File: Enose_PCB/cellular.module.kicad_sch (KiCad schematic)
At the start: 40 parts, among them J7 U.FL-R-SMT_01_, J8 U.FL-R-SMT_01_, J9 2229333-2, Q1 Q_NPN, Q2 Q_NPN, Q3 Q_NPN, Q4 Q_NPN, Q5 Q_NPN, U4 SIM7070G

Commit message: Changed power symbols
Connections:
- net +BATT renamed +SYS_SW
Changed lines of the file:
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@@
 		(on_board yes)
 		(dnp no)
-		(fields_autoplaced yes)
-		(property "Reference" "#PWR0109"
+		(property "Reference" "#PWR090"
 			(at 229.87 33.02 0)
 			(effects
@@
 			)
 		)
-		(property "Value" "+BATT"
-			(at 237.49 33.0199 90)
+		(property "Value" "+SYS_SW"
+			(at 236.474 33.02 90)
 			(effects
 				(font
@@
 		)
 		(instances
-			(project ""
-				(path "/bf99c0e6-4ae6-4f18-a827-087a9b51b368"
-					(reference "#PWR08")
+			(project "Enose_PCB"
+				(path "/eef70be0-4107-491c-8ca0-465071a6397e/2117c019-44e0-44cf-b334-dcd1316d0701"
+					(reference "#PWR090")
 					(unit 1)
 				)
 			)
+		)
+	)
+	(symbol
+		(lib_id "power:+BATT")
+		(at 214.63 116.84 0)
+		(unit 1)
+		(exclude_from_sim no)
+		(in_bom yes)
+		(on_board yes)
+		(dnp no)
+		(property "Reference" "#PWR091"
+			(at 214.63 120.65 0)
+			(effects
+				(font
+					(size 1.27 1.27)
+				)
+				(hide yes)
+			)
+		)
+		(property "Value" "+SYS_SW"
+			(at 210.566 112.522 0)
+			(effects
+				(font
+					(size 1.27 1.27)
+				)
+				(justify left)
+			)
+		)
+		(property "Footprint" ""
+			(at 214.63 116.84 0)
+			(effects
+				(font
+					(size 1.27 1.27)
+				)
+				(hide yes)
+			)
+		)
+		(property "Datasheet" ""
+			(at 214.63 116.84 0)
+			(effects
+				(font
+					(size 1.27 1.27)
+				)
+				(hide yes)
+			)
+		)
+		(property "Description" "Power symbol creates a global label with name \"+BATT\""
+			(at 214.63 116.84 0)
+			(effects
+				(font
+					(size 1.27 1.27)
+				)
+				(hide yes)
+			)
+		)
+		(pin "1"
+		)
+		(instances
 			(project "Enose_PCB"
 				(path "/eef70be0-4107-491c-8ca0-465071a6397e/2117c019-44e0-44cf-b334-dcd1316d0701"
-					(reference "#PWR0109")
+					(reference "#PWR091")
 					(unit 1)
 				)
@@
 	)
 	(symbol
-		(lib_id "power:+BATT")
-		(at 266.7 116.84 0)
-		(unit 1)
-		(exclude_from_sim no)
-		(in_bom yes)
-		(on_board yes)
-		(dnp no)
-		(fields_autoplaced yes)
-		(property "Reference" "#PWR018"
-			(at 266.7 120.65 0)
-			(effects
-				(font
-					(size 1.27 1.27)
-				)
-				(hide yes)
-			)
-		)
-		(property "Value" "+BATT"
-			(at 266.7 111.76 0)
-			(effects
-				(font
-					(size 1.27 1.27)
-				)
-			)
-		)
-		(property "Footprint" ""
-			(at 266.7 116.84 0)
-			(effects
-				(font
-					(size 1.27 1.27)
-				)
-				(hide yes)
-			)
-		)
-		(property "Datasheet" ""
-			(at 266.7 116.84 0)
-			(effects
-				(font
-					(size 1.27 1.27)
-				)
-				(hide yes)
-			)
-		)
-		(property "Description" "Power symbol creates a global label with name \"+BATT\""
-			(at 266.7 116.84 0)
-			(effects
-				(font
-					(size 1.27 1.27)
-				)
-				(hide yes)
-			)
-		)
-		(pin "1"
-		)
-		(instances
-			(project "Enose_PCB"
-				(path "/eef70be0-4107-491c-8ca0-465071a6397e/2117c019-44e0-44cf-b334-dcd1316d0701"
-					(reference "#PWR018")
-					(unit 1)
-				)
-			)
-		)
-	)
-	(symbol
 		(lib_id "U.FL-R-SMT_01_:U.FL-R-SMT_01_")
 		(at 55.88 102.87 0)
@@
 	)
 	(symbol
+		(lib_id "power:+BATT")
+		(at 266.7 116.84 0)
+		(unit 1)
+		(exclude_from_sim no)
+		(in_bom yes)
+		(on_board yes)
+		(dnp no)
+		(property "Reference" "#PWR018"
+			(at 266.7 120.65 0)
+			(effects
+				(font
+					(size 1.27 1.27)
+				)
+				(hide yes)
+			)
+		)
+		(property "Value" "+SYS_SW"
+			(at 262.636 112.522 0)
+			(effects
+				(font
+					(size 1.27 1.27)
+				)
+				(justify left)
+			)
+		)
+		(property "Footprint" ""
+			(at 266.7 116.84 0)
+			(effects
+				(font
+					(size 1.27 1.27)
+				)
+				(hide yes)
+			)
+		)
+		(property "Datasheet" ""
+			(at 266.7 116.84 0)
+			(effects
+				(font
+					(size 1.27 1.27)
+				)
+				(hide yes)
+			)
+		)
+		(property "Description" "Power symbol creates a global label with name \"+BATT\""
+			(at 266.7 116.84 0)
+			(effects
+				(font
+					(size 1.27 1.27)
+				)
+				(hide yes)
+			)
+		)
+		(pin "1"
+		)
+		(instances
+			(project "Enose_PCB"
+				(path "/eef70be0-4107-491c-8ca0-465071a6397e/2117c019-44e0-44cf-b334-dcd1316d0701"
+					(reference "#PWR018")
+					(unit 1)
+				)
+			)
+		)
+	)
+	(symbol
 		(lib_id "power:GND")
 		(at 184.15 24.13 180)
@@
 					(unit 1)
 				)
-			)
-		)
-	)
-	(symbol
-		(lib_id "power:+BATT")
-		(at 214.63 116.84 0)
-		(unit 1)
-		(exclude_from_sim no)
-		(in_bom yes)
-		(on_board yes)
-		(dnp no)
-		(fields_autoplaced yes)
-		(property "Reference" "#PWR019"
-			(at 214.63 120.65 0)
-			(effects
-				(font
-					(size 1.27 1.27)
-				)
-				(hide yes)
-			)
-		)
-		(property "Value" "+BATT"
-			(at 214.63 111.76 0)
-			(effects
-				(font
-					(size 1.27 1.27)
-				)
-			)
-		)
-		(property "Footprint" ""
-			(at 214.63 116.84 0)
-			(effects
-				(font
-					(size 1.27 1.27)
-				)
-				(hide yes)
-			)
-		)
-		(property "Datasheet" ""
-			(at 214.63 116.84 0)
-			(effects
-				(font
-					(size 1.27 1.27)
-				)
-				(hide yes)
-			)
-		)
-		(property "Description" "Power symbol creates a global label with name \"+BATT\""
-			(at 214.63 116.84 0)
-			(effects
-				(font
-					(size 1.27 1.27)
-				)
-				(hide yes)
-			)
-		)
-		(pin "1"
-		)
-		(instances
-			(project "Enose_PCB"
-				(path "/eef70be0-4107-491c-8ca0-465071a6397e/2117c019-44e0-44cf-b334-dcd1316d0701"
-					(reference "#PWR019")
-					(unit 1)
-				)

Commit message: Working on Enose PCB Layout
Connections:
- net GND: now also Q1.2 (E), Q4.2 (E), Q5.2 (E); no longer Q1.E, Q4.E, Q5.E
- net UART1_RXD: now also Q2.2 (E); no longer Q2.E
- net UART1_TXD: now also Q3.3 (C); no longer Q3.C
- net at R16.2, R17.2: now also Q1.1 (B); no longer Q1.B
- net at C26.2, R20.1, U4.10 (UART1_RXD): now also Q2.3 (C); no longer Q2.C
- net at R27.2, R28.2: now also Q5.1 (B); no longer Q5.B
- net at R19.2: now also Q3.1 (B); no longer Q3.B
- net at U4.9 (UART1_TXD): now also Q3.2 (E); no longer Q3.E
- net at R18.2: now also Q2.1 (B); no longer Q2.B
- net at R25.2: now also Q4.3 (C); no longer Q4.C
- net at U4.1 (PWRKEY): now also Q1.3 (C); no longer Q1.C
- net at R21.2, R22.2: now also Q4.1 (B); no longer Q4.B
- net at R29.2: now also Q5.3 (C); no longer Q5.C
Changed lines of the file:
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@@
 		)
 	)
+	(netclass_flag ""
+		(length 2.54)
+		(shape round)
+		(at 157.48 33.02 0)
+		(fields_autoplaced yes)
+		(effects
+			(font
+				(size 1.27 1.27)
+			)
+			(justify left bottom)
+		)
+		(property "Netclass" "POWER_2A"
+			(at 158.1785 30.48 0)
+			(effects
+				(font
+					(size 1.27 1.27)
+				)
+				(justify left)
+				(hide yes)
+			)
+		)
+		(property "Component Class" ""
+			(at -109.22 0 0)
+			(effects
+				(font
+					(size 1.27 1.27)
+					(italic yes)
+				)
+			)
+		)
+	)
 	(symbol
 		(lib_id "power:GND")
@@
 			)
 		)
-		(pin "E"
+		(pin "1"
 		)
-		(pin "C"
+		(pin "3"
 		)
-		(pin "B"
+		(pin "2"
 		)
 		(instances
@@
 	)
 	(symbol
+		(lib_name "Q_NPN_4")
 		(lib_id "Device:Q_NPN")
 		(at 73.66 58.42 270)
@@
 			)
 		)
-		(pin "E"
+		(pin "2"
 		)
-		(pin "C"
+		(pin "1"
 		)
-		(pin "B"
+		(pin "3"
 		)
 		(instances
@@
 	)
 	(symbol
+		(lib_name "Q_NPN_3")
 		(lib_id "Device:Q_NPN")
 		(at 54.61 40.64 0)
@@
 			)
 		)
-		(pin "E"
+		(pin "1"
 		)
-		(pin "C"
+		(pin "3"
 		)
-		(pin "B"
+		(pin "2"
 		)
 		(instances
@@
 	)
 	(symbol
+		(lib_name "Q_NPN_2")
 		(lib_id "Device:Q_NPN")
 		(at 264.16 139.7 0)
@@
 			)
 		)
-		(pin "E"
+		(pin "2"
 		)
-		(pin "C"
+		(pin "3"
 		)
-		(pin "B"
+		(pin "1"
 		)
 		(instances
@@
 	)
 	(symbol
+		(lib_name "Q_NPN_1")
 		(lib_id "Device:Q_NPN")
 		(at 212.09 139.7 0)
@@
 			)
 		)
-		(pin "E"
+		(pin "1"
 		)
-		(pin "C"
+		(pin "3"
 		)
-		(pin "B"
+		(pin "2"
 		)
 		(instances

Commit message: Enose PCB almost done
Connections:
- net UART1_RXD: now also Q3.3 (C); no longer Q2.2 (E)
- net UART1_TXD: now also Q2.2 (E); no longer Q3.3 (C)
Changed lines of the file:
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@@
+	(wire
+		(pts
+			(xy 266.7 144.78) (xy 266.7 148.59)
+		)
+		(stroke
+			(width 0)
+			(type default)
+		)
+	)
+	(wire
+		(pts
+			(xy 101.6 91.44) (xy 102.87 91.44)
+		)
+		(stroke
+			(width 0)
+			(type default)
+		)
+	)
+	(wire
+		(pts
+			(xy 266.7 148.59) (xy 266.7 149.86)
+		)
+		(stroke
+			(width 0)
+			(type default)
+		)
+	)
+	(wire
+		(pts
+			(xy 163.83 31.75) (xy 163.83 33.02)
+		)
+		(stroke
+			(width 0)
+			(type default)
+		)
+	)
+	(wire
+		(pts
+			(xy 86.36 46.99) (xy 73.66 46.99)
+		)
+		(stroke
+			(width 0)
+			(type default)
+		)
+	)
+	(wire
+		(pts
+			(xy 223.52 63.5) (xy 223.52 66.04)
+		)
+		(stroke
+			(width 0)
+			(type default)
+		)
+	)
+	(wire
+		(pts
+			(xy 198.12 68.58) (xy 208.28 68.58)
+		)
+		(stroke
+			(width 0)
+			(type default)
+		)
+	)
+	(wire
+		(pts
+			(xy 254 148.59) (xy 254 139.7)
+		)
+		(stroke
+			(width 0)
+			(type default)
+		)
+	)
+	(wire
+		(pts
+			(xy 219.71 73.66) (xy 228.6 73.66)
+		)
+		(stroke
+			(width 0)
+			(type default)
+		)
+	)
+	(wire
+		(pts
+			(xy 86.36 60.96) (xy 96.52 60.96)
+		)
+		(stroke
+			(width 0)
+			(type default)
+		)
+	)
+	(wire
+		(pts
+			(xy 102.87 66.04) (xy 99.06 66.04)
+		)
+		(stroke
+			(width 0)
+			(type default)
+		)
+	)
+	(wire
+		(pts
+			(xy 186.69 68.58) (xy 190.5 68.58)
+		)
+		(stroke
+			(width 0)
+			(type default)
+		)
+	)
+	(wire
+		(pts
+			(xy 99.06 68.58) (xy 93.98 68.58)
+		)
+		(stroke
+			(width 0)
+			(type default)
+		)
+	)
+	(wire
+		(pts
+			(xy 163.83 33.02) (xy 173.99 33.02)
+		)
+		(stroke
+			(width 0)
+			(type default)
+		)
+	)
+	(wire
+		(pts
+			(xy 266.7 148.59) (xy 261.62 148.59)
+		)
+		(stroke
+			(width 0)
+			(type default)
+		)
+	)
+	(wire
+		(pts
+			(xy 274.32 71.12) (xy 274.32 73.66)
+		)
+		(stroke
+			(width 0)
+			(type default)
+		)
+	)
+	(wire
+		(pts
+			(xy 203.2 78.74) (xy 203.2 83.82)
+		)
+		(stroke
+			(width 0)
+			(type default)
+		)
+	)
+	(wire
+		(pts
+			(xy 152.4 35.56) (xy 152.4 33.02)
+		)
+		(stroke
+			(width 0)
+			(type default)
+		)
+	)
+	(wire
+		(pts
+			(xy 44.45 100.33) (xy 45.72 100.33)
+		)
+		(stroke
+			(width 0)
+			(type default)
+		)
+	)
+	(wire
+		(pts
+			(xy 184.15 33.02) (xy 195.58 33.02)
+		)
+		(stroke
+			(width 0)
+			(type default)
+		)
+	)
 	(wire
 		(pts
@@
 	(wire
 		(pts
-			(xy 266.7 144.78) (xy 266.7 148.59)
-		)
-		(stroke
-			(width 0)
-			(type default)
-		)
-	)
-	(wire
-		(pts
-			(xy 101.6 91.44) (xy 102.87 91.44)
-		)
-		(stroke
-			(width 0)
-			(type default)
-		)
-	)
-	(wire
-		(pts
-			(xy 266.7 148.59) (xy 266.7 149.86)
-		)
-		(stroke
-			(width 0)
-			(type default)
-		)
-	)
-	(wire
-		(pts
-			(xy 163.83 31.75) (xy 163.83 33.02)
-		)
-		(stroke
-			(width 0)
-			(type default)
-		)
-	)
-	(wire
-		(pts
-			(xy 86.36 46.99) (xy 73.66 46.99)
-		)
-		(stroke
-			(width 0)
-			(type default)
-		)
-	)
-	(wire
-		(pts
-			(xy 223.52 63.5) (xy 223.52 66.04)
-		)
-		(stroke
-			(width 0)
-			(type default)
-		)
-	)
-	(wire
-		(pts
-			(xy 198.12 68.58) (xy 208.28 68.58)
-		)
-		(stroke
-			(width 0)
-			(type default)
-		)
-	)
-	(wire
-		(pts
-			(xy 254 148.59) (xy 254 139.7)
-		)
-		(stroke
-			(width 0)
-			(type default)
-		)
-	)
-	(wire
-		(pts
-			(xy 219.71 73.66) (xy 228.6 73.66)
-		)
-		(stroke
-			(width 0)
-			(type default)
-		)
-	)
-	(wire
-		(pts
-			(xy 86.36 60.96) (xy 96.52 60.96)
-		)
-		(stroke
-			(width 0)
-			(type default)
-		)
-	)
-	(wire
-		(pts
-			(xy 102.87 66.04) (xy 99.06 66.04)
-		)
-		(stroke
-			(width 0)
-			(type default)
-		)
-	)
-	(wire
-		(pts
-			(xy 186.69 68.58) (xy 190.5 68.58)
-		)
-		(stroke
-			(width 0)
-			(type default)
-		)
-	)
-	(wire
-		(pts
-			(xy 99.06 68.58) (xy 93.98 68.58)
-		)
-		(stroke
-			(width 0)
-			(type default)
-		)
-	)
-	(wire
-		(pts
-			(xy 163.83 33.02) (xy 173.99 33.02)
-		)
-		(stroke
-			(width 0)
-			(type default)
-		)
-	)
-	(wire
-		(pts
-			(xy 266.7 148.59) (xy 261.62 148.59)
-		)
-		(stroke
-			(width 0)
-			(type default)
-		)
-	)
-	(wire
-		(pts
-			(xy 274.32 71.12) (xy 274.32 73.66)
-		)
-		(stroke
-			(width 0)
-			(type default)
-		)
-	)
-	(wire
-		(pts
-			(xy 203.2 78.74) (xy 203.2 83.82)
-		)
-		(stroke
-			(width 0)
-			(type default)
-		)
-	)
-	(wire
-		(pts
-			(xy 152.4 35.56) (xy 152.4 33.02)
-		)
-		(stroke
-			(width 0)
-			(type default)
-		)
-	)
-	(wire
-		(pts
-			(xy 44.45 100.33) (xy 45.72 100.33)
-		)
-		(stroke
-			(width 0)
-			(type default)
-		)
-	)
-	(wire
-		(pts
-			(xy 184.15 33.02) (xy 195.58 33.02)
-		)
-		(stroke
-			(width 0)
-			(type default)
-		)
-	)
-	(wire
-		(pts
 			(xy 224.79 33.02) (xy 229.87 33.02)
 		)
@@
 	(wire
 		(pts
+			(xy 64.77 68.58) (xy 83.82 68.58)
+		)
+		(stroke
+			(width 0)
+			(type default)
+		)
+	)
+	(wire
+		(pts
 			(xy 101.6 86.36) (xy 102.87 86.36)
 		)
@@
 		(pts
 			(xy 148.59 114.3) (xy 148.59 116.84)
-		)
-		(stroke
-			(width 0)
-			(type default)
-		)
-	)
-	(wire
-		(pts
-			(xy 64.77 68.58) (xy 83.82 68.58)
 		)
 		(stroke
@@
 	(global_label "UART1_TXD"
 		(shape input)
-		(at 64.77 68.58 180)
+		(at 64.77 60.96 180)
 		(fields_autoplaced yes)
 		(effects
@@
 		)
 		(property "Intersheetrefs" "${INTERSHEET_REFS}"
-			(at 51.5039 68.58 0)
+			(at 51.5039 60.96 0)
 			(effects
 				(font
@@
 	(global_label "UART1_RXD"
 		(shape input)
-		(at 64.77 60.96 180)
+		(at 64.77 68.58 180)
 		(fields_autoplaced yes)
 		(effects
@@
 		)
 		(property "Intersheetrefs" "${INTERSHEET_REFS}"
-			(at 51.2015 60.96 0)
+			(at 51.2015 68.58 0)
 			(effects
 				(font

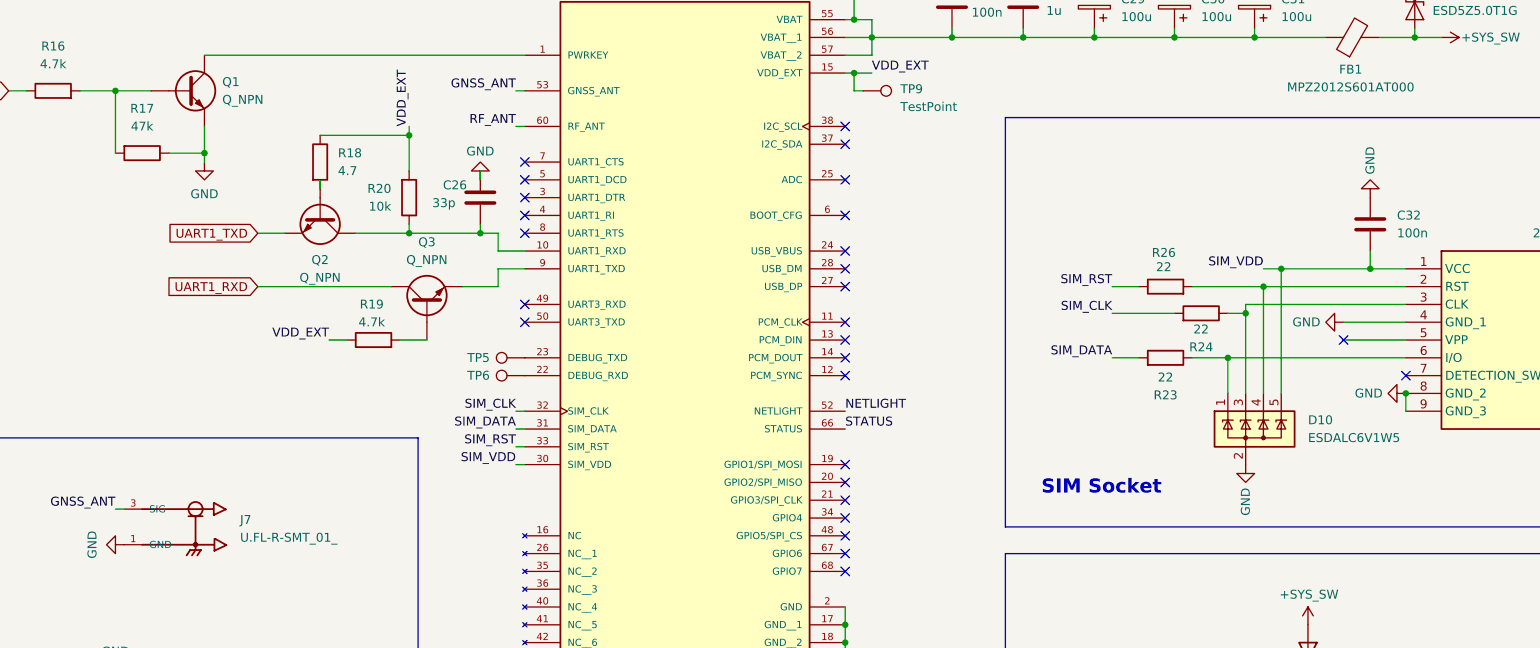
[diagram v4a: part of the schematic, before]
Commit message: Enose PCB almost done, just needs ground vias
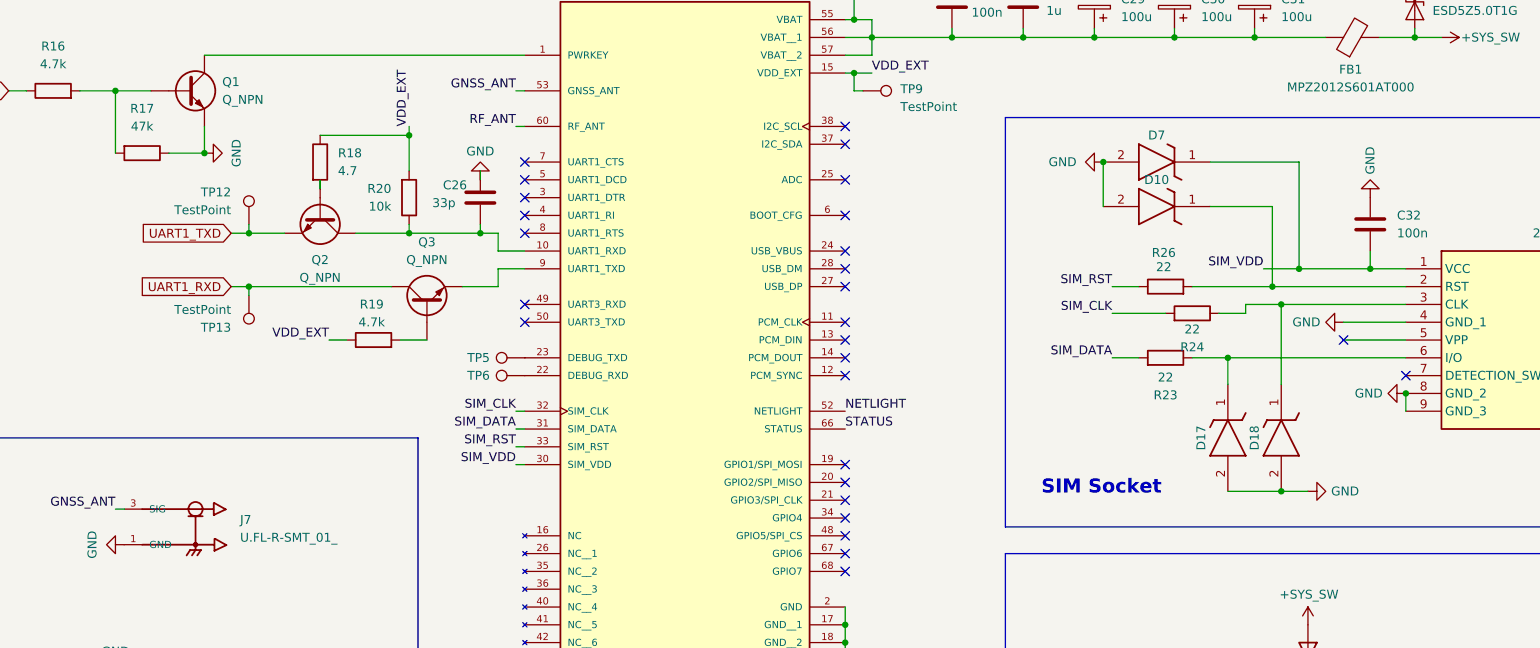
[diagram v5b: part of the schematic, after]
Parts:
- removed D10: ESDALC6V1W5, ESDALC6V1W5:SOT65P210X110-5N, symbol Power_Protection:SP0504BAHT
- added D10, D17, D18, D7: ESD8351XV2T1G, SamacSys_Parts:SODFL1608X70N, symbol SamacSys_Parts:ESD8351XV2T1G
- added TP12, TP13: TestPoint, TestPoint:TestPoint_Pad_D1.5mm, symbol Connector:TestPoint
- TP5, TP6, TP8, TP9: footprint TestPoint:TestPoint_Pad_1.5x1.5mm -> TestPoint:TestPoint_Pad_D1.5mm
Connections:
- net GND: now also D10.2 (A), D17.2 (A), D18.2 (A), D7.2 (A)
- net SIM_VDD: now also D7.1 (K)
- net UART1_RXD: now also TP13.1
- net UART1_TXD: now also TP12.1
- net at J9.3 (CLK), R24.1: now also D18.1 (K)
- net at J9.2 (RST), R26.2: now also D10.1 (K)
- net at J9.6 (I/O), R23.1: now also D17.1 (K)
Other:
- moved on the sheet: R24
